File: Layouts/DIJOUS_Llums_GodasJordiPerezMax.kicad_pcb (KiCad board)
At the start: 2 copper layers, 85.1 x 69 mm, 103 parts, among them J1 Conn_01x05_Socket, J2 Conn_01x03, J3 Conn_01x06, J4 Screw_Terminal_01x02, J5 Conn_01x05, J6 DE9_Plug, J7 Conn_01x02, J8 Conn_01x06_Socket, K1 G5LE-1 DC12, K2 G5LE-1 DC12, Q1 ZXTN19020DFFTA, Q2 ZXTN19020DFFTA, Q3 ZXTN19020DFFTA, Q4 Si7336ADP, Q5 Si7336ADP, Q6 ZXTN19020DFFTA, Q7 ZXTN19020DFFTA, Q8 Si7336ADP, Q9 Si7336ADP, U1 PCA9306D, U2 PIC18F2580-I/SO, U3 LM2596T-ADJ, U5 MCP2551-I-SN, U6 ADM7172ACPZ-5.0-R7, U7 LT6202CS5, U8 TLV1117-33

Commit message: Add files via upload
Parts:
- moved C14 18.3 mm to (102.6, 70.6)
- moved R45 2.10 mm to (105.4, 74.6)
- moved R43 1.25 mm to (107.6, 76.5), turned to -90 degrees
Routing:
- net Motor_in2: track 10.9 -> 13.7 mm
- net /NMOSbase12: track 5.26 -> 4.01 mm

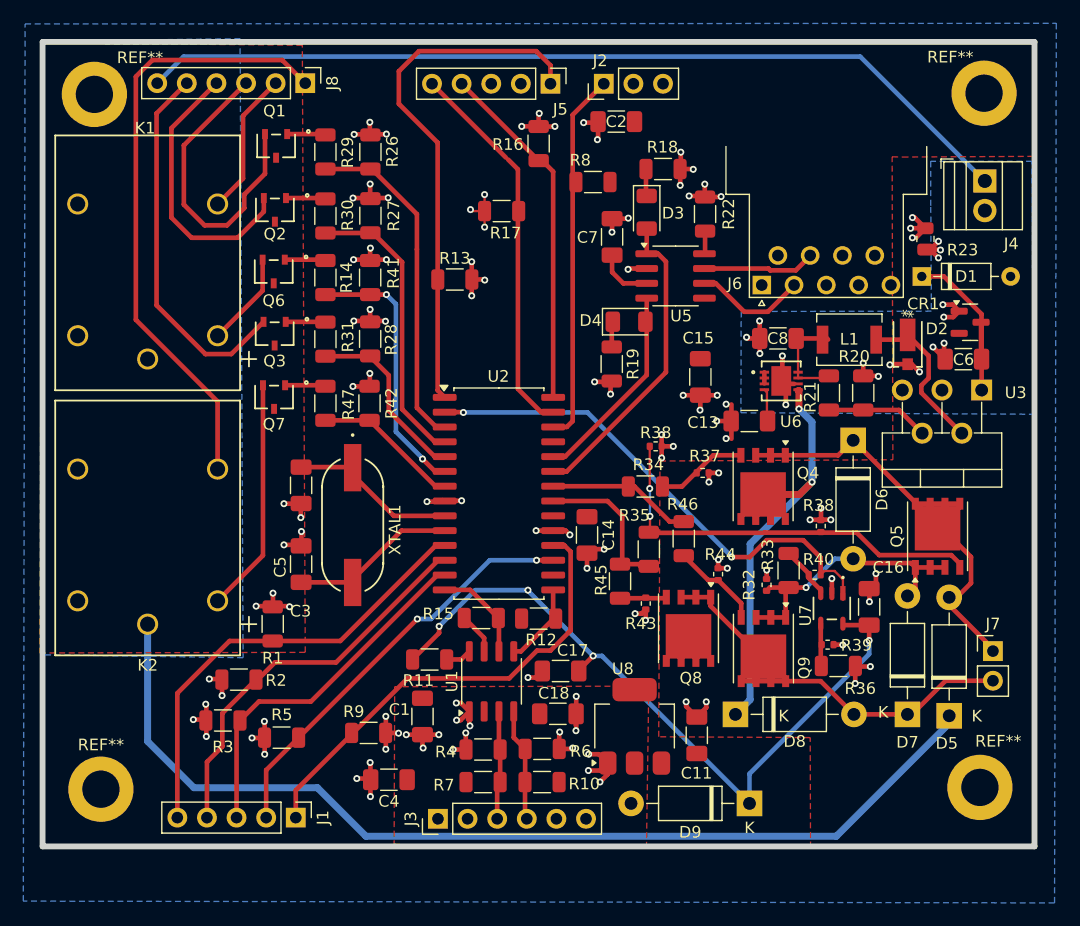
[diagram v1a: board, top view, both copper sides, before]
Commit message: Update PCB
S'ha reorganitzat la zona de potència gràcies a un forat que ha deixat el DB-9. S'han col·locat les noves footprints canviades
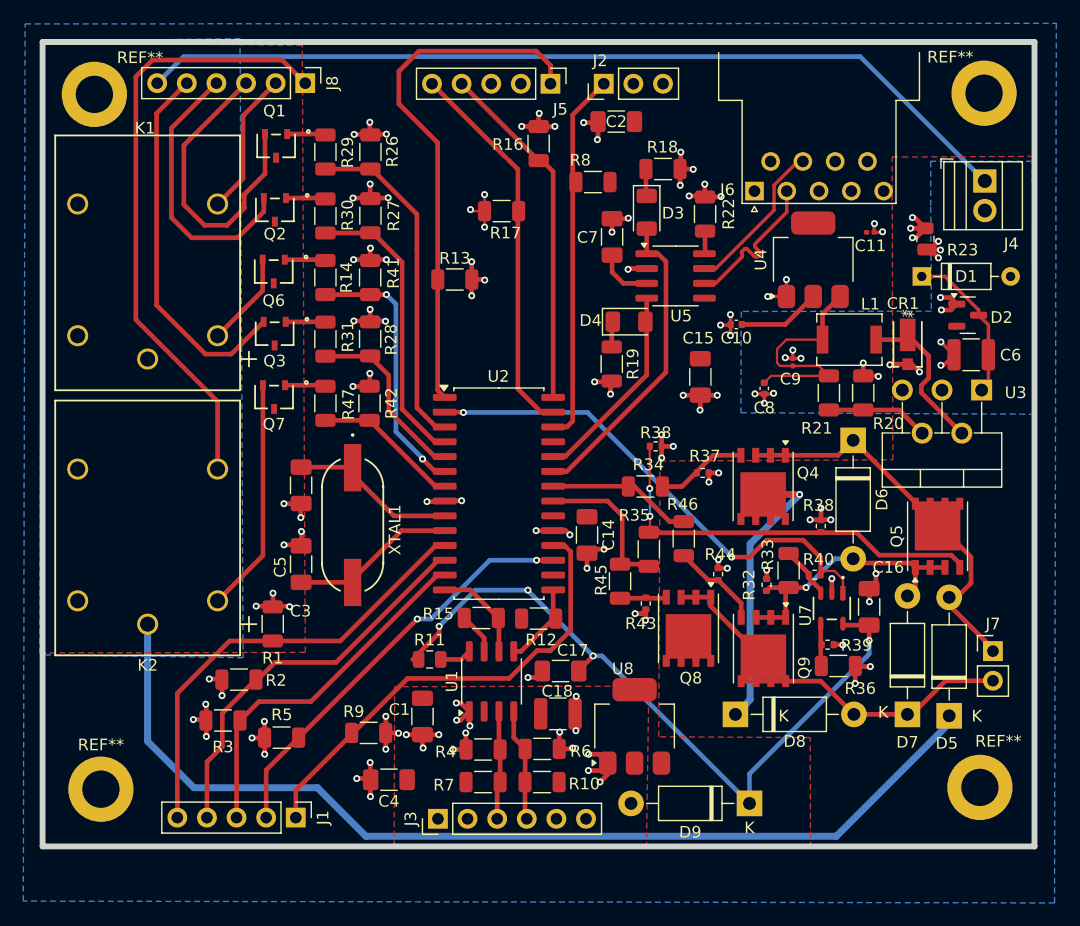
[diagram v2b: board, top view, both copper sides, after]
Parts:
- removed C13: 1nF, Capacitor_SMD:C_1206_3216Metric_Pad1.33x1.80mm_HandSolder
- removed U6: ADM7172ACPZ-5.0-R7, ADM7172ACPZ-5.0-R7:CP-8-21_ADI
- added C10: 22u, Capacitor_SMD:C_0402_1005Metric, F.Cu at (115.4, 52.5)
- added C9: 10u, Capacitor_SMD:C_0201_0603Metric, F.Cu at (120.2, 55.8)
- added U4: LT1117-5.0, Package_TO_SOT_SMD:SOT-223-3_TabPin2, F.Cu at (122.0, 47.0)
- C11: footprint Capacitor_SMD:C_1206_3216Metric_Pad1.33x1.80mm_HandSolder -> Capacitor_SMD:C_0201_0603Metric
- C18, C6: footprint Capacitor_SMD:C_1206_3216Metric_Pad1.33x1.80mm_HandSolder -> Capacitor_SMD:C_1210_3225Metric
- C8: footprint Capacitor_SMD:C_1206_3216Metric_Pad1.33x1.80mm_HandSolder -> Capacitor_SMD:C_0402_1005Metric
- R11: footprint Resistor_SMD:R_1206_3216Metric -> Capacitor_SMD:C_0805_2012Metric
- R20: value 2.49k -> 2k
- R21: value 6.49k -> 6.81k
- moved C11 45.6 mm to (126.9, 44.6), turned to 0 degrees
- moved J6 8.08 mm to (117.0, 41.1)
- moved C8 4.44 mm to (117.8, 58.0), turned to -90 degrees
- moved C6 0.77 mm to (135.6, 55.1)
- moved D2 0.64 mm to (135.2, 51.8)
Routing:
- net /LDO5V_IN: track 8.97 -> 20.8 mm
- net +12V: track 122.3 -> 110.9 mm, vias 2 -> 1
- net +5V: track 73.1 -> 79.3 mm
- net GNDPWR: track 101.3 -> 96.5 mm, vias 16 -> 17
- net CANH_O: track 9.66 -> 13.5 mm
- net CANL_O: track 9.65 -> 13.4 mm
- net /SS5V: track 3.27 -> 0.00 mm
- net /Buck_IN: track 16.5 -> 13.5 mm
- net GND: track 147.3 -> 147.1 mm, vias 109 -> 111

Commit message: Add files via upload
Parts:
- C3, C5: footprint Capacitor_SMD:C_1206_3216Metric_Pad1.33x1.80mm_HandSolder -> Capacitor_SMD:C_0603_1608Metric
- moved C3 0.84 mm to (78.1, 65.5)
- moved C5 0.62 mm to (78.1, 73.7)
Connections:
- net Net-(U5-Rs) renamed /TRANS_Rs
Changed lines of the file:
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@@
 	(net 60 "SCL_O")
 	(net 61 "/NMOSbase22")
-	(net 62 "Net-(U5-Rs)")
+	(net 62 "/TRANS_Rs")
 	(net 63 "/ENABLE")
 	(net 64 "/Buck_FB")
@@
 			(layers "F.Cu" "F.Paste" "F.Mask")
 			(roundrect_rratio 0.222222)
-			(net 62 "Net-(U5-Rs)")
+			(net 62 "/TRANS_Rs")
 			(pintype "passive")
 		)
@@
 		)
 		(fp_text user "${REFERENCE}"
-			(at 0 0 360)
+			(at 0 0 0)
 			(layer "F.Fab")
 			(effects
@@
 			(layers "F.Cu" "F.Paste" "F.Mask")
 			(roundrect_rratio 0.25)
-			(net 62 "Net-(U5-Rs)")
+			(net 62 "/TRANS_Rs")
 			(pinfunction "Rs")
 			(pintype "input")
@@
 		)
 		(property "Value" "10uF"
-			(at 0 1.05 360)
+			(at 0 1.05 0)
 			(layer "F.Fab")
 			(effects
@@
 		)
 		(fp_text user "${REFERENCE}"
-			(at 0 -0.68 360)
+			(at 0 -0.68 0)
 			(layer "F.Fab")
 			(effects
@@
 		)
 	)
-	(footprint "Capacitor_SMD:C_1206_3216Metric_Pad1.33x1.80mm_HandSolder"
+	(footprint "Capacitor_SMD:C_0603_1608Metric"
 		(layer "F.Cu")
-		(at 78.0796 73.1012 90)
-		(descr "Capacitor SMD 1206 (3216 Metric), square (rectangular) end terminal, IPC_7351 nominal with elongated pad for handsoldering. (Body size source: IPC-SM-782 page 76, https://www.pcb-3d.com/wordpress/wp-content/uploads/ipc-sm-782a_amendment_1_and_2.pdf), generated with kicad-footprint-generator")
-		(tags "capacitor handsolder")
+		(at 78.0796 73.725 90)
+		(descr "Capacitor SMD 0603 (1608 Metric), square (rectangular) end terminal, IPC_7351 nominal, (Body size source: IPC-SM-782 page 76, https://www.pcb-3d.com/wordpress/wp-content/uploads/ipc-sm-782a_amendment_1_and_2.pdf), generated with kicad-footprint-generator")
+		(tags "capacitor")
 		(property "Reference" "C5"
-			(at -0.255101 -1.795 90)
+			(at 0 -1.43 90)
 			(layer "F.SilkS")
 			(effects
@@
 		)
 		(property "Value" "56pF"
-			(at 0 1.85 90)
+			(at 0 1.43 90)
 			(layer "F.Fab")
 			(effects
@@
 			)
 		)
-		(property "Footprint" "Capacitor_SMD:C_1206_3216Metric_Pad1.33x1.80mm_HandSolder"
+		(property "Footprint" "Capacitor_SMD:C_0603_1608Metric"
 			(at 0 0 90)
 			(unlocked yes)
@@
 		(attr smd)
 		(fp_line
-			(start -0.711252 -0.91)
-			(end 0.711252 -0.91)
+			(start -0.14058 -0.51)
+			(end 0.14058 -0.51)
 			(stroke
 				(width 0.12)
@@
 		)
 		(fp_line
-			(start -0.711252 0.91)
-			(end 0.711252 0.91)
+			(start -0.14058 0.51)
+			(end 0.14058 0.51)
 			(stroke
 				(width 0.12)
@@
 		)
 		(fp_line
-			(start 2.48 -1.15)
-			(end 2.48 1.15)
+			(start 1.48 -0.73)
+			(end 1.48 0.73)
 			(stroke
 				(width 0.05)
@@
 		)
 		(fp_line
-			(start -2.48 -1.15)
-			(end 2.48 -1.15)
+			(start -1.48 -0.73)
+			(end 1.48 -0.73)
 			(stroke
 				(width 0.05)
@@
 		)
 		(fp_line
-			(start 2.48 1.15)
-			(end -2.48 1.15)
+			(start 1.48 0.73)
+			(end -1.48 0.73)
 			(stroke
 				(width 0.05)
@@
 		)
 		(fp_line
-			(start -2.48 1.15)
-			(end -2.48 -1.15)
+			(start -1.48 0.73)
+			(end -1.48 -0.73)
 			(stroke
 				(width 0.05)
@@
 		)
 		(fp_line
-			(start 1.6 -0.8)
-			(end 1.6 0.8)
+			(start 0.8 -0.4)
+			(end 0.8 0.4)
 			(stroke
 				(width 0.1)
@@
 		)
 		(fp_line
-			(start -1.6 -0.8)
-			(end 1.6 -0.8)
+			(start -0.8 -0.4)
+			(end 0.8 -0.4)
 			(stroke
 				(width 0.1)
@@
 		)
 		(fp_line
-			(start 1.6 0.8)
-			(end -1.6 0.8)
+			(start 0.8 0.4)
+			(end -0.8 0.4)
 			(stroke
 				(width 0.1)
@@
 		)
 		(fp_line
-			(start -1.6 0.8)
-			(end -1.6 -0.8)
+			(start -0.8 0.4)
+			(end -0.8 -0.4)
 			(stroke
 				(width 0.1)
@@
 			(effects
 				(font
-					(size 0.8 0.8)
-					(thickness 0.12)
+					(size 0.4 0.4)
+					(thickness 0.06)
 				)
 			)
 		)
 		(pad "1" smd roundrect
-			(at -1.5625 0 90)
-			(size 1.325 1.8)
+			(at -0.775 0 90)
+			(size 0.9 0.95)
 			(layers "F.Cu" "F.Paste" "F.Mask")
-			(roundrect_rratio 0.188679)
+			(roundrect_rratio 0.25)
 			(net 71 "/OSC2")
 			(pintype "passive")
 		)
 		(pad "2" smd roundrect
-			(at 1.5625 0 90)
-			(size 1.325 1.8)
+			(at 0.775 0 90)
+			(size 0.9 0.95)
 			(layers "F.Cu" "F.Paste" "F.Mask")
-			(roundrect_rratio 0.188679)
+			(roundrect_rratio 0.25)
 			(net 1 "GND")
 			(pintype "passive")
 		)
-		(model "${KICAD8_3DMODEL_DIR}/Capacitor_SMD.3dshapes/C_1206_3216Metric.wrl"
+		(model "${KICAD8_3DMODEL_DIR}/Capacitor_SMD.3dshapes/C_0603_1608Metric.wrl"
 			(offset
 				(xyz 0 0 0)
@@
 		)
 	)
-	(footprint "Capacitor_SMD:C_1206_3216Metric_Pad1.33x1.80mm_HandSolder"
+	(footprint "Capacitor_SMD:C_0603_1608Metric"
 		(layer "F.Cu")
-		(at 78.0796 66.3448 -90)
-		(descr "Capacitor SMD 1206 (3216 Metric), square (rectangular) end terminal, IPC_7351 nominal with elongated pad for handsoldering. (Body size source: IPC-SM-782 page 76, https://www.pcb-3d.com/wordpress/wp-content/uploads/ipc-sm-782a_amendment_1_and_2.pdf), generated with kicad-footprint-generator")
-		(tags "capacitor handsolder")
+		(at 78.0796 65.5 -90)
+		(descr "Capacitor SMD 0603 (1608 Metric), square (rectangular) end terminal, IPC_7351 nominal, (Body size source: IPC-SM-782 page 76, https://www.pcb-3d.com/wordpress/wp-content/uploads/ipc-sm-782a_amendment_1_and_2.pdf), generated with kicad-footprint-generator")
+		(tags "capacitor")
 		(property "Reference" "C3"
-			(at 10.790099 0.049 0)
+			(at 0 -1.43 -90)
 			(layer "F.SilkS")
 			(effects
@@
 		)
 		(property "Value" "56pF"
-			(at 1.778 1.088 90)
+			(at 0 1.43 -90)
 			(layer "F.Fab")
 			(effects
@@
 			)
 		)
-		(property "Footprint" "Capacitor_SMD:C_1206_3216Metric_Pad1.33x1.80mm_HandSolder"
+		(property "Footprint" "Capacitor_SMD:C_0603_1608Metric"
 			(at 0 0 -90)
 			(unlocked yes)
@@
 		(attr smd)
 		(fp_line
-			(start -0.711252 0.91)
-			(end 0.711252 0.91)
+			(start -0.14058 0.51)
+			(end 0.14058 0.51)
 			(stroke
 				(width 0.12)
@@
 		)
 		(fp_line
-			(start -0.711252 -0.91)
-			(end 0.711252 -0.91)
+			(start -0.14058 -0.51)
+			(end 0.14058 -0.51)
 			(stroke
 				(width 0.12)
@@
 		)
 		(fp_line
-			(start -2.48 1.15)
-			(end -2.48 -1.15)
+			(start -1.48 0.73)
+			(end -1.48 -0.73)
 			(stroke
 				(width 0.05)
@@
 		)
 		(fp_line
-			(start 2.48 1.15)
-			(end -2.48 1.15)
+			(start 1.48 0.73)
+			(end -1.48 0.73)
 			(stroke
 				(width 0.05)
@@
 		)
 		(fp_line
-			(start -2.48 -1.15)
-			(end 2.48 -1.15)
+			(start -1.48 -0.73)
+			(end 1.48 -0.73)
 			(stroke
 				(width 0.05)
@@
 		)
 		(fp_line
-			(start 2.48 -1.15)
-			(end 2.48 1.15)
+			(start 1.48 -0.73)
+			(end 1.48 0.73)
 			(stroke
 				(width 0.05)
@@
 		)
 		(fp_line
-			(start -1.6 0.8)
-			(end -1.6 -0.8)
+			(start -0.8 0.4)
+			(end -0.8 -0.4)
 			(stroke
 				(width 0.1)
@@
 		)
 		(fp_line
-			(start 1.6 0.8)
-			(end -1.6 0.8)
+			(start 0.8 0.4)
+			(end -0.8 0.4)
 			(stroke
 				(width 0.1)
@@
 		)
 		(fp_line
-			(start -1.6 -0.8)
-			(end 1.6 -0.8)
+			(start -0.8 -0.4)
+			(end 0.8 -0.4)
 			(stroke
 				(width 0.1)
@@
 		)
 		(fp_line
-			(start 1.6 -0.8)
-			(end 1.6 0.8)
+			(start 0.8 -0.4)
+			(end 0.8 0.4)
 			(stroke
 				(width 0.1)
@@
 		)
 		(fp_text user "${REFERENCE}"
-			(at 0 0 90)
+			(at 0 0 -90)
 			(layer "F.Fab")
 			(effects
 				(font
-					(size 0.8 0.8)
-					(thickness 0.12)
+					(size 0.4 0.4)
+					(thickness 0.06)
 				)
 			)
 		)
 		(pad "1" smd roundrect
-			(at -1.5625 0 270)
-			(size 1.325 1.8)
+			(at -0.775 0 270)
+			(size 0.9 0.95)
 			(layers "F.Cu" "F.Paste" "F.Mask")
-			(roundrect_rratio 0.188679)
+			(roundrect_rratio 0.25)
 			(net 70 "/OSC1")
 			(pintype "passive")
 		)
 		(pad "2" smd roundrect
-			(at 1.5625 0 270)
-			(size 1.325 1.8)
+			(at 0.775 0 270)
+			(size 0.9 0.95)
 			(layers "F.Cu" "F.Paste" "F.Mask")
-			(roundrect_rratio 0.188679)
+			(roundrect_rratio 0.25)
 			(net 1 "GND")
 			(pintype "passive")
 		)
-		(model "${KICAD8_3DMODEL_DIR}/Capacitor_SMD.3dshapes/C_1206_3216Metric.wrl"
+		(model "${KICAD8_3DMODEL_DIR}/Capacitor_SMD.3dshapes/C_0603_1608Metric.wrl"
 			(offset
 				(xyz 0 0 0)
@@
 		(tags "capacitor")
 		(property "Reference" "C10"
-			(at 0 -1.16 360)
+			(at 0 -1.16 0)
 			(layer "F.SilkS")
 			(effects
@@
 		)
 		(property "Value" "22u"
-			(at 0 1.16 360)
+			(at 0 1.16 0)
 			(layer "F.Fab")
 			(effects
@@
 		)
 		(fp_text user "${REFERENCE}"
-			(at 0 0 360)
+			(at 0 0 0)
 			(layer "F.Fab")
 			(effects
@@
 	)
 	(segment
-		(start 78.0542 69.1134)
-		(end 78.0542 67.9327)
+		(start 78.0542 67.5)
+		(end 78.0542 66.3193)
 		(width 0.4)
 		(layer "F.Cu")
@@
 	)
 	(segment
-		(start 76.6064 67.9196)
-		(end 78.0673 67.9196)
+		(start 76.6064 66.3062)
+		(end 78.0673 66.3062)
 		(width 0.4)
 		(layer "F.Cu")
@@
 	)
 	(segment
-		(start 78.105 71.5133)
-		(end 78.0796 71.5387)
-		(width 0.4)
-		(layer "F.Cu")
-		(net 1)
-	)
-	(segment
 		(start 125.603 83.3374)
 		(end 125.603 81.8535)
@@
 	)
 	(segment
-		(start 77.9911 71.4502)
-		(end 78.0796 71.5387)
-		(width 0.4)
-		(layer "F.Cu")
-		(net 1)
-	)
-	(segment
 		(start 88.48695 88.81715)
 		(end 88.5444 88.8746)
@@
 	)
 	(segment
-		(start 76.6064 71.4502)
-		(end 77.9911 71.4502)
+		(start 76.6064 73.03995)
+		(end 77.9911 73.03995)
 		(width 0.4)
 		(layer "F.Cu")
@@
 	)
 	(segment
-		(start 78.105 70.3072)
-		(end 78.105 71.5133)
+		(start 78.105 71.89695)
+		(end 78.105 73.10305)
 		(width 0.4)
 		(layer "F.Cu")
@@
 	)
 	(via
-		(at 78.0542 69.1134)
+		(at 78.0542 67.5)
 		(size 0.6)
 		(drill 0.3)
@@
 	)
 	(via
-		(at 76.6064 67.9196)
+		(at 76.6064 66.3062)
 		(size 0.6)
 		(drill 0.3)
@@
 	)
 	(via
-		(at 76.6064 71.4502)
+		(at 76.6064 73.03995)
 		(size 0.6)
 		(drill 0.3)
@@
 	)
 	(via
-		(at 78.105 70.3072)
+		(at 78.105 71.89695)
 		(size 0.6)
 		(drill 0.3)
